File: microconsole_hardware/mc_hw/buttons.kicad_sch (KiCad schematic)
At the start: 33 parts, among them SW10 TL3301NF160QG, SW11 TL3301NF160QG, SW12 TL3301NF160QG, SW13 TL3301NF160QG, SW14 TL3301NF160QG, SW15 TL3301NF160QG, SW16 Joystick, SW17 Joystick, SW2 TL3301NF160QG, SW3 TL3301NF160QG, SW4 TL3301NF160QG, SW5 TL3301NF160QG, SW6 TL3301NF160QG, SW7 TL3301NF160QG, SW8 TL3301NF160QG, SW9 TL3301NF160QG, U3 MCP23017-E/SO, U4 ADS7828E/2K5

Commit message: fix a bunch of footprints and routing
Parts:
- FB1: footprint PCM_SparkFun-Capacitor:C_0603_1608Metric -> Ferrite_THT:LairdTech_28C0236-0JW-10
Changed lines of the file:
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@@
 			)
 		)
-		(property "Footprint" "PCM_SparkFun-Capacitor:C_0603_1608Metric"
+		(property "Footprint" "Ferrite_THT:LairdTech_28C0236-0JW-10"
 			(at 269.24 47.752 90)
 			(hide yes)

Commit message: fix up
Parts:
- FB1: footprint Ferrite_THT:LairdTech_28C0236-0JW-10 -> (none)
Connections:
- net MCP RESET: no longer names the net of R11.1, U3.18 (~{RESET})
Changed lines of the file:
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@@
 	)
 	(junction
-		(at 147.32 68.58)
+		(at 212.09 30.48)
 		(diameter 0)
 		(color 0 0 0 0)
 	)
 	(junction
-		(at 243.84 87.63)
+		(at 147.32 68.58)
 		(diameter 0)
 		(color 0 0 0 0)
 	)
 	(junction
-		(at 132.08 177.8)
+		(at 243.84 87.63)
 		(diameter 0)
 		(color 0 0 0 0)
 	)
 	(junction
-		(at 137.16 172.72)
+		(at 132.08 177.8)
 		(diameter 0)
 		(color 0 0 0 0)
@@
 	(wire
 		(pts
-			(xy 218.44 33.02) (xy 212.09 33.02)
+			(xy 218.44 30.48) (xy 212.09 30.48)
 		)
 		(stroke
@@
 	(wire
 		(pts
-			(xy 139.7 172.72) (xy 137.16 172.72)
-		)
-		(stroke
-			(width 0)
-			(type default)
-		)
-	)
-	(wire
-		(pts
 			(xy 132.08 68.58) (xy 135.89 68.58)
 		)
@@
 	(wire
 		(pts
-			(xy 137.16 172.72) (xy 130.81 172.72)
+			(xy 212.09 30.48) (xy 212.09 33.02)
 		)
 		(stroke
@@
 	(wire
 		(pts
-			(xy 143.51 68.58) (xy 147.32 68.58)
+			(xy 137.16 172.72) (xy 130.81 172.72)
 		)
 		(stroke
@@
 	(wire
 		(pts
-			(xy 199.39 27.94) (xy 196.85 27.94)
+			(xy 143.51 68.58) (xy 147.32 68.58)
 		)
 		(stroke
@@
 	(wire
 		(pts
-			(xy 228.6 68.58) (xy 232.41 68.58)
+			(xy 199.39 27.94) (xy 196.85 27.94)
 		)
 		(stroke
@@
 	(wire
 		(pts
-			(xy 212.09 30.48) (xy 212.09 33.02)
+			(xy 228.6 68.58) (xy 232.41 68.58)
 		)
 		(stroke
@@
 	(global_label "GND"
 		(shape input)
-		(at 218.44 33.02 0)
+		(at 218.44 30.48 0)
 		(fields_autoplaced yes)
 		(effects
@@
 		)
 		(property "Intersheetrefs" "${INTERSHEET_REFS}"
-			(at 225.2957 33.02 0)
+			(at 225.2957 30.48 0)
 			(hide yes)
 			(show_name no)
@@
 		)
 	)
-	(global_label "MCP RESET"
-		(shape input)
-		(at 139.7 172.72 0)
-		(fields_autoplaced yes)
-		(effects
-			(font
-				(size 1.27 1.27)
-			)
-			(justify left)
-		)
-		(property "Intersheetrefs" "${INTERSHEET_REFS}"
-			(at 153.3893 172.72 0)
-			(hide yes)
-			(show_name no)
-			(do_not_autoplace no)
-			(effects
-				(font
-					(size 1.27 1.27)
-				)
-				(justify left)
-			)
-		)
-	)
 	(global_label "IO0 {slash} Left Stick X"
 		(shape input)
@@
 		)
 		(property "Voltage" "25V"
-			(at 216.662 46.482 0)
+			(at 210.82 49.53 0)
 			(show_name no)
 			(do_not_autoplace no)
@@
 					(size 1.27 1.27)
 				)
-				(justify left)
 			)
 		)
 		(property "Tolerance" "20%"
-			(at 212.598 46.482 0)
+			(at 210.82 52.07 0)
 			(show_name no)
 			(do_not_autoplace no)
@@
 					(size 1.27 1.27)
 				)
-				(justify left)
 			)
 		)
@@
 			)
 		)
-		(property "Footprint" "Ferrite_THT:LairdTech_28C0236-0JW-10"
+		(property "Footprint" ""
 			(at 269.24 47.752 90)
 			(hide yes)
@@
 	)
 	(symbol
+		(lib_name "GINFULL_HallEffect_Joystick_PTH_1")
 		(lib_id "project_parts:GINFULL_HallEffect_Joystick_PTH")
 		(at 147.32 109.22 0)
@@
 	)
 	(symbol
-		(lib_name "GINFULL_HallEffect_Joystick_PTH_1")
 		(lib_id "project_parts:GINFULL_HallEffect_Joystick_PTH")
 		(at 243.84 109.22 0)

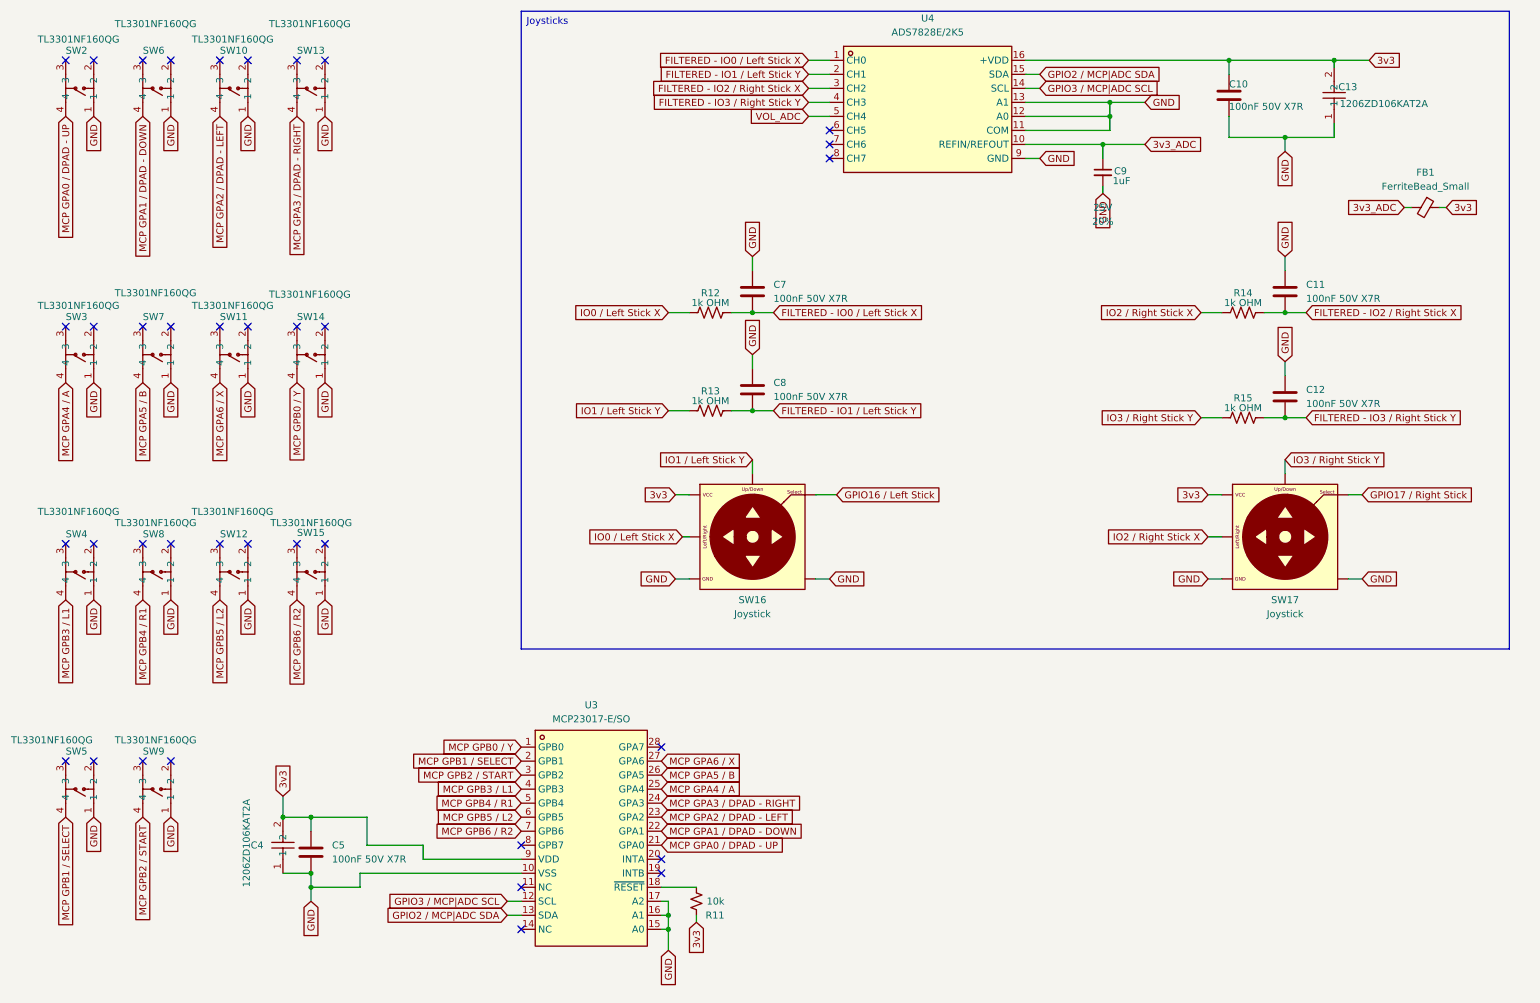
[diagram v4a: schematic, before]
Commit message: fix ferrite beads.
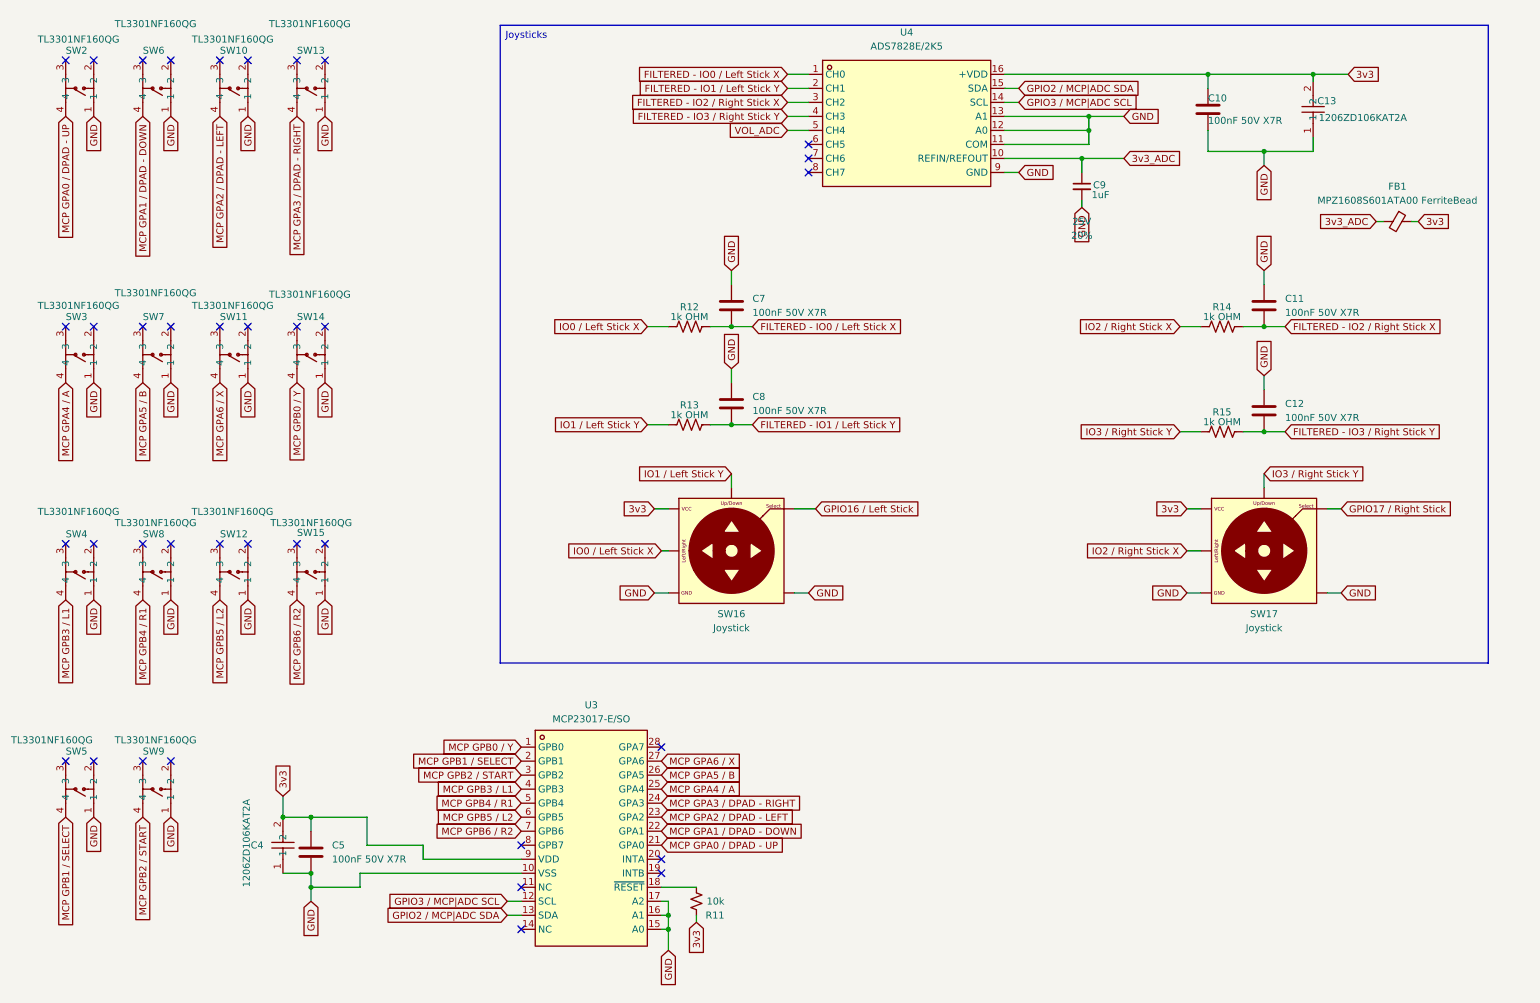
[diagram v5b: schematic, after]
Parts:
- FB1: value FerriteBead_Small -> MPZ1608S601ATA00 FerriteBead; footprint (none) -> Inductor_SMD:L_0603_1608Metric_Pad1.05x0.95mm_HandSolder
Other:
- moved on the sheet: C10, C11, C12, C13, C7, C8, C9, FB1, R12, R13, R14, R15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

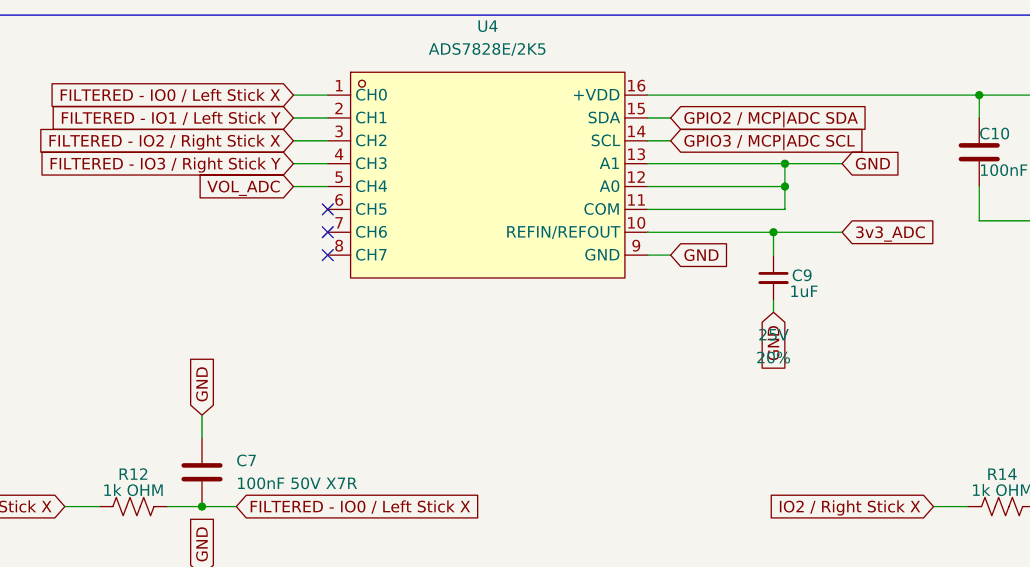
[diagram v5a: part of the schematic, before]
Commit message: add battery sense and thermistor
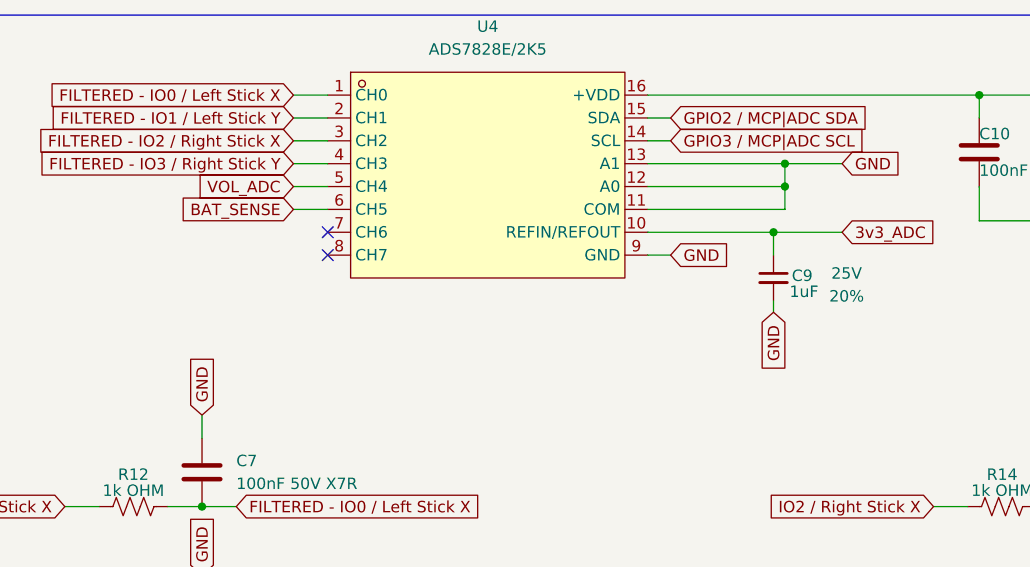
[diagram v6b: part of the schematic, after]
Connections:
- net BAT_SENSE: now reaches U4.6 (CH5)
- no-connect marks 37 -> 36
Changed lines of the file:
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@@
-	)
-	(no_connect
-		(at 157.48 38.1)
 	)
 	(no_connect
@@
 	(wire
 		(pts
+			(xy 153.67 38.1) (xy 157.48 38.1)
+		)
+		(stroke
+			(width 0)
+			(type default)
+		)
+	)
+	(wire
+		(pts
 			(xy 67.31 172.72) (xy 67.31 175.26)
 		)
@@
 				)
 				(justify left)
+			)
+		)
+	)
+	(global_label "BAT_SENSE"
+		(shape input)
+		(at 153.67 38.1 180)
+		(fields_autoplaced yes)
+		(effects
+			(font
+				(size 1.27 1.27)
+			)
+			(justify right)
+		)
+		(property "Intersheetrefs" "${INTERSHEET_REFS}"
+			(at 140.3435 38.1 0)
+			(hide yes)
+			(show_name no)
+			(do_not_autoplace no)
+			(effects
+				(font
+					(size 1.27 1.27)
+				)
+				(justify right)
 			)
 		)
@@
 		)
 		(property "Voltage" "25V"
-			(at 207.01 52.07 0)
+			(at 215.138 45.212 0)
 			(show_name no)
 			(do_not_autoplace no)
@@
 		)
 		(property "Tolerance" "20%"
-			(at 207.01 54.61 0)
-			(show_name no)
-			(do_not_autoplace no)
+			(at 215.138 47.752 0)
+			(show_name no)
+			(do_not_autoplace no)
